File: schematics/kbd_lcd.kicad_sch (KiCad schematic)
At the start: 41 parts, among them J2 Mini-DIN-6, Q1 2N3906, U1 74HC04, U12 74HC04, U13 74HC125, U14 74HC14, U15 NE555P, U16 74HC04, U17 74HC595, U18 80x4 Character LCD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

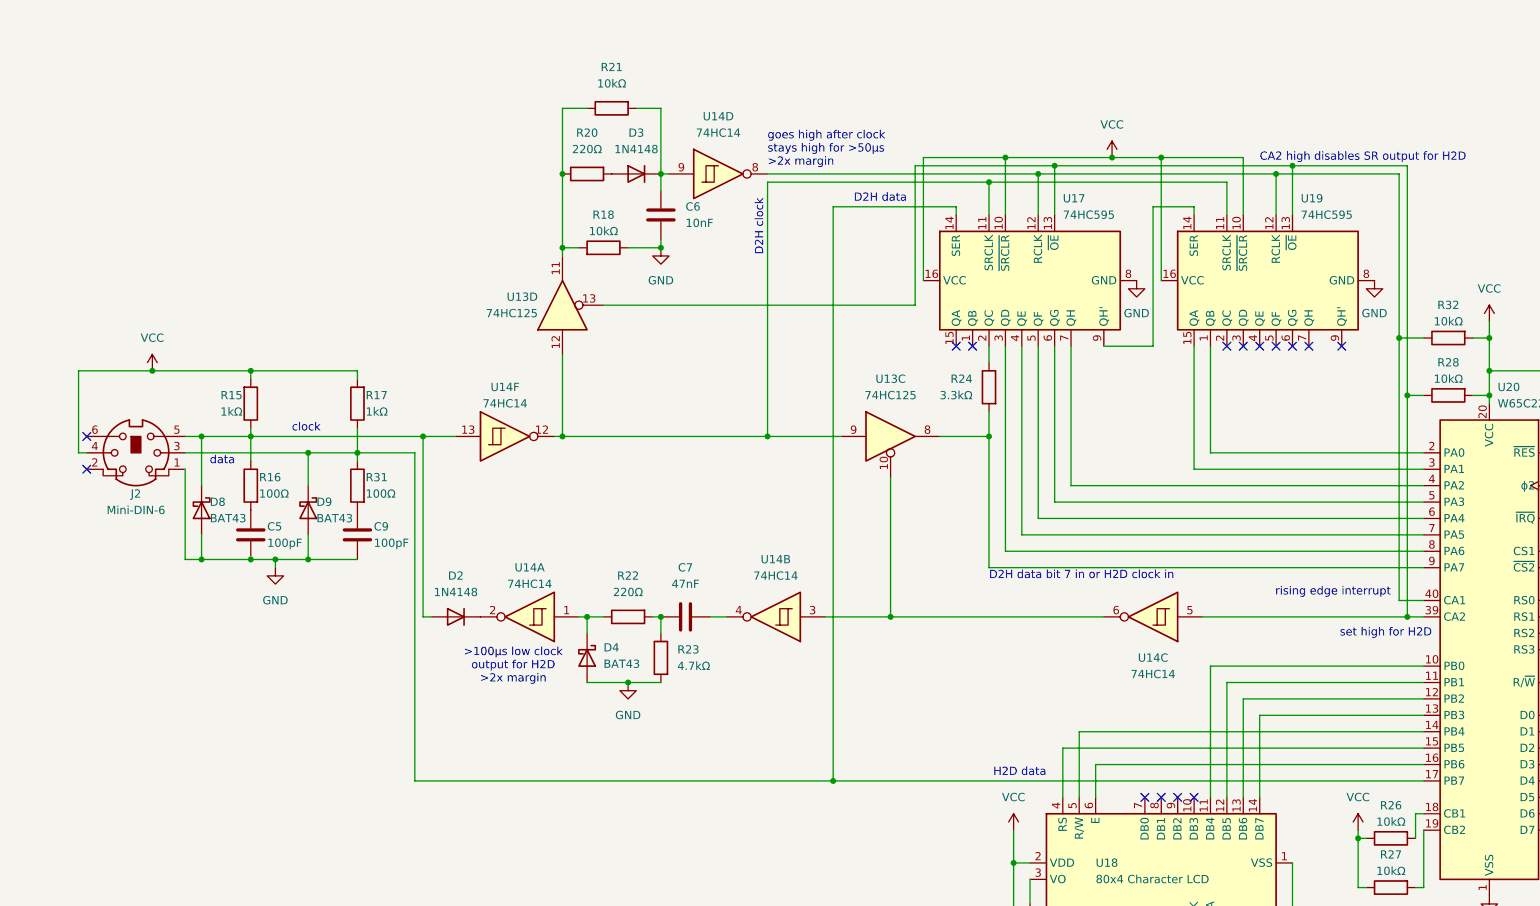
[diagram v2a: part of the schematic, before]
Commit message: LCD works with 4 MHz PHI2
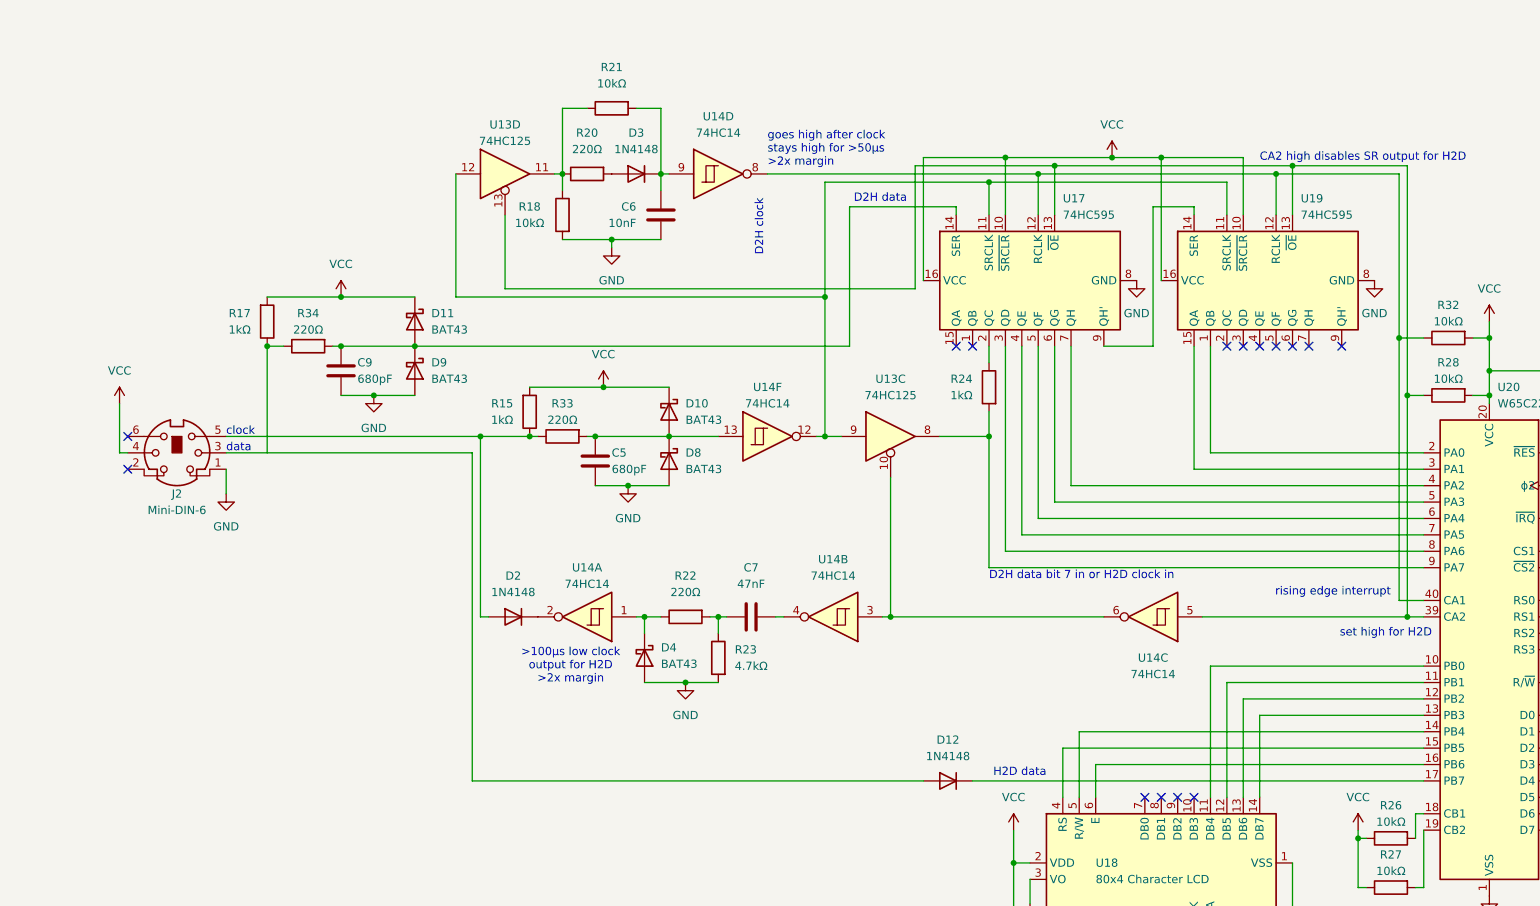
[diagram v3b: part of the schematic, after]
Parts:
- removed R16, R31: 100Ω, symbol Device:R
- added D10, D11: BAT43, Diode_THT:D_DO-35_SOD27_P7.62mm_Horizontal, symbol Diode:BAT43
- added D12: 1N4148, Diode_THT:D_DO-35_SOD27_P7.62mm_Horizontal, symbol Diode:1N4148
- added R33, R34: 220Ω, symbol Device:R
- C5, C9: value 100pF -> 680pF
- R24: value 3.3kΩ -> 1kΩ
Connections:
- net GND: now also R18.2; no longer R18.1
- net VCC: now also D10.1 (K), D11.1 (K)
- net at R20.1, R21.1, U13.11: now also R18.1; no longer R18.2
- net at D2.2 (A), J2.5, R15.1: now also R33.1; no longer D8.1 (K), U14.13
- net at C9.1: now also D9.1 (K), U17.14 (SER), D11.2 (A), R34.2
- net at C5.1: now also D8.1 (K), U14.13, D10.2 (A), R33.2
- new net: D12.2 (A), J2.3
- new net: R17.1, R34.1
- new net: D12.1 (K), U20.17 (PB7)
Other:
- moved on the sheet: C7, D2, D4, J2, R15, R17, R18, R22, R23, U14A, U14B, U14F
